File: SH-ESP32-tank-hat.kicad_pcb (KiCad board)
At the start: 4 copper layers, 83 x 55.5 mm, 37 parts, among them J302 GPIO, J303 I2C, J304 Conn_01x02, J305 Power

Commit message: Initial PCB layout
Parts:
- removed the G*** at (78.8, 85.4)
- added C401: 100nF, Capacitor_SMD:C_0402_1005Metric, F.Cu at (107.7, 70.0)
- added C402: 100nF, Capacitor_SMD:C_0402_1005Metric, F.Cu at (107.7, 80.2)
- added C403: 100nF, Capacitor_SMD:C_0402_1005Metric, F.Cu at (122.8, 79.0)
- added C404: 68nF, Capacitor_SMD:C_0603_1608Metric, F.Cu at (127.2, 75.6)
- added C405: 100nF, Capacitor_SMD:C_0402_1005Metric, F.Cu at (107.7, 90.5)
- added C406: 100nF, Capacitor_SMD:C_0402_1005Metric, F.Cu at (107.7, 100.5)
- added C407: 1uF, Capacitor_SMD:C_0402_1005Metric, F.Cu at (118.3, 86.6)
- added C408: 1uF, Capacitor_SMD:C_0402_1005Metric, F.Cu at (115.8, 88.1)
- added C409: 1uF, Capacitor_SMD:C_0402_1005Metric, F.Cu at (115.7, 92.1)
- added C410: 1uF, Capacitor_SMD:C_0402_1005Metric, F.Cu at (117.3, 95.4)
- added C411: 100nF, Capacitor_SMD:C_0402_1005Metric, F.Cu at (118.8, 95.1)
- added C501: 47nF, Capacitor_SMD:C_0603_1608Metric, F.Cu at (133.4, 106.8)
- added C502: 4.7nF, Capacitor_SMD:C_0603_1608Metric, F.Cu at (127.4, 107.0)
- added D501: BZT52C16S, Diode_SMD:D_SOD-323, F.Cu at (131.6, 107.0)
- added J301: GPIO_bottom, Connector_PinSocket_2.54mm:PinSocket_2x20_P2.54mm_Vertical, F.Cu at (167.6, 61.3)
- added J306: Opto, Connector_PinSocket_2.54mm:PinSocket_1x04_P2.54mm_Vertical, B.Cu at (128.3, 113.2)
- added J307: 1-Wire_top, Connector_PinSocket_2.54mm:PinSocket_1x03_P2.54mm_Vertical, F.Cu at (150.3, 102.5)
- added J308: 1-Wire_bottom, Connector_PinSocket_2.54mm:PinSocket_1x03_P2.54mm_Vertical, B.Cu at (150.3, 113.2)
- added J401: Conn_01x02, Connector_Phoenix_MC:PhoenixContact_MCV_1,5_2-G-3.81_1x02_P3.81mm_Vertical, F.Cu at (93.8, 83.0)
- added J402: Conn_01x02, Connector_Phoenix_MC:PhoenixContact_MCV_1,5_2-G-3.81_1x02_P3.81mm_Vertical, F.Cu at (93.8, 72.6)
- added J403: Conn_01x02, Connector_Phoenix_MC:PhoenixContact_MCV_1,5_2-G-3.81_1x02_P3.81mm_Vertical, F.Cu at (93.8, 93.2)
- added J404: Conn_01x02, Connector_Phoenix_MC:PhoenixContact_MCV_1,5_2-G-3.81_1x02_P3.81mm_Vertical, F.Cu at (93.8, 103.4)
- added J501: Conn_01x02, Connector_Phoenix_MC:PhoenixContact_MCV_1,5_2-G-3.81_1x02_P3.81mm_Vertical, F.Cu at (134.4, 100.4)
- added JP501: SolderJumper_2_Open, Jumper:SolderJumper-2_P1.3mm_Open_Pad1.0x1.5mm, F.Cu at (136.2, 108.4)
- added Q401: S9015, Package_TO_SOT_SMD:SOT-23, F.Cu at (103.7, 69.0)
- added Q402: S9015, Package_TO_SOT_SMD:SOT-23, F.Cu at (103.7, 79.2)
- added Q403: S9015, Package_TO_SOT_SMD:SOT-23, F.Cu at (103.7, 89.5)
- added Q404: S9015, Package_TO_SOT_SMD:SOT-23, F.Cu at (103.7, 99.5)
- added R401: 1k, Resistor_SMD:R_0402_1005Metric, F.Cu at (106.7, 70.0)
- added R402: 1k, Resistor_SMD:R_0402_1005Metric, F.Cu at (106.7, 80.2)
- added R403: 30, Resistor_SMD:R_0603_1608Metric, F.Cu at (107.7, 68.0)
- added R404: 30, Resistor_SMD:R_0603_1608Metric, F.Cu at (107.7, 78.2)
- added R405: 1k, Resistor_SMD:R_0402_1005Metric, F.Cu at (129.0, 76.5)
- added R406: 10k, Resistor_SMD:R_0402_1005Metric, F.Cu at (129.0, 75.4)
- added R407: 1k, Resistor_SMD:R_0402_1005Metric, F.Cu at (106.7, 90.5)
- added R408: 1k, Resistor_SMD:R_0402_1005Metric, F.Cu at (106.7, 100.5)
- added R409: 30, Resistor_SMD:R_0603_1608Metric, F.Cu at (107.7, 88.5)
- added R410: 30, Resistor_SMD:R_0603_1608Metric, F.Cu at (107.7, 98.5)
- added R411: 1.5k, Resistor_SMD:R_0402_1005Metric, F.Cu at (117.3, 86.6)
- added R412: 1.5k, Resistor_SMD:R_0402_1005Metric, F.Cu at (115.8, 89.1)
- added R413: 1.5k, Resistor_SMD:R_0402_1005Metric, F.Cu at (115.7, 93.1)
- added R414: 1.5k, Resistor_SMD:R_0402_1005Metric, F.Cu at (117.3, 94.4)
- added R501: 3.3k, Resistor_SMD:R_0805_2012Metric, F.Cu at (129.4, 107.0)
- added U401: LMV324, Package_SO:SOIC-14_3.9x8.7mm_P1.27mm, F.Cu at (117.5, 79.0)
- added U402: ADS1115IDGS, Package_SO:TSSOP-10_3x3mm_P0.5mm, F.Cu at (118.7, 90.7)
- J302: value GPIO -> I2C_top; footprint Connector_PinHeader_2.54mm:PinHeader_2x20_P2.54mm_Vertical -> Connector_PinHeader_2.54mm:PinHeader_1x04_P2.54mm_Vertical
- J303: value I2C -> I2C_bottom; moved to B.Cu
- J304: value Conn_01x02 -> Vin_Prot; footprint Connector_PinHeader_2.54mm:PinHeader_1x02_P2.54mm_Vertical -> Connector_PinSocket_2.54mm:PinSocket_1x02_P2.54mm_Vertical; moved to B.Cu
- J305: footprint Connector_PinHeader_2.54mm:PinHeader_2x03_P2.54mm_Vertical -> Connector_PinSocket_2.54mm:PinSocket_2x03_P2.54mm_Vertical; moved to B.Cu
- moved J302 42.0 mm to (150.3, 97.1)
- turned J303 to 90 degrees
- turned J304 to 270 degrees
- turned J305 to 90 degrees
- renumbered C1001 to C201, C1002 to C202, C1003 to C203, C1004 to C204, C1005 to C205, C1006 to C206, C1007 to C207, C1008 to C208, C1009 to C209, C1010 to C210, C1011 to C211, C1012 to C212, C1013 to C213, C1014 to C214, C1015 to C215, C1016 to C216, C1017 to C217, C1018 to C218, C1019 to C219, C1020 to C220, C1021 to C221, C1022 to C222, C1023 to C223, C1024 to C224, C1025 to C225, C1026 to C226, C1027 to C227, C1028 to C228, H1001 to H201, H1002 to H202
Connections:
- J302 pad 1: (no net) -> GND
- J302 pad 2: (no net) -> +3V3
- J302 pad 3: (no net) -> /SCL
- J302 pad 4: (no net) -> /SDA
- J303 pad 3: (no net) -> /SCL
- J303 pad 4: (no net) -> /SDA
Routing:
- net /Tank sender/VoutA: track 0.00 -> 43.5 mm, vias 0 -> 2
- net /Tank sender/Vin: track 0.00 -> 41.7 mm, vias 0 -> 6
- net /SCL: track 0.00 -> 39.0 mm
- net /SDA: track 0.00 -> 36.3 mm
- net Net-(Q401-Pad1): track 0.00 -> 34.9 mm, vias 0 -> 2
- net /Tank sender/VoutB: track 0.00 -> 33.5 mm, vias 0 -> 4
- net Net-(C401-Pad1): track 0.00 -> 33.2 mm, vias 0 -> 2
- net Net-(Q403-Pad1): track 0.00 -> 31.4 mm, vias 0 -> 2
- net Net-(Q404-Pad1): track 0.00 -> 30.8 mm, vias 0 -> 2
- net /Tank sender/VoutD: track 0.00 -> 30.4 mm, vias 0 -> 2
- net Net-(C406-Pad1): track 0.00 -> 29.6 mm, vias 0 -> 2
- net Net-(C402-Pad1): track 0.00 -> 27.7 mm, vias 0 -> 4
- net /Tank sender/VoutC: track 0.00 -> 26.6 mm, vias 0 -> 2
- net Net-(C405-Pad1): track 0.00 -> 24.0 mm, vias 0 -> 2
- net Net-(Q402-Pad1): track 0.00 -> 22.4 mm, vias 0 -> 2
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- added copper zone on B.Cu, net +3V3
- added copper zone on F.Cu, net GND
- added copper zone on B.Cu, net ISO_GND
- added copper zone on F.Cu, net ISO_GND
- removed copper zone on In2.Cu, net +3V3
- removed copper zone on In1.Cu, net GND
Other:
- board size 83 x 55.5 mm -> 83 x 58 mm
- copper layers 4 -> 2
- board text added: "1Wire"
- board text added: "DQ"
- board text added: "Tach"
- board text added: "Tank A"
- board text added: "Tank B"
- board text added: "Tank C"
- board text added: "Tank D"
- board text removed: "Revision 0.3.0"
- board text removed: "Sailor Hat with ESP32"
- board text removed: "VIn Prot"
- board text removed: "Vin Prot"
- board text removed: "https://github.com/hatlabs/SH-ESP32-hardware/"

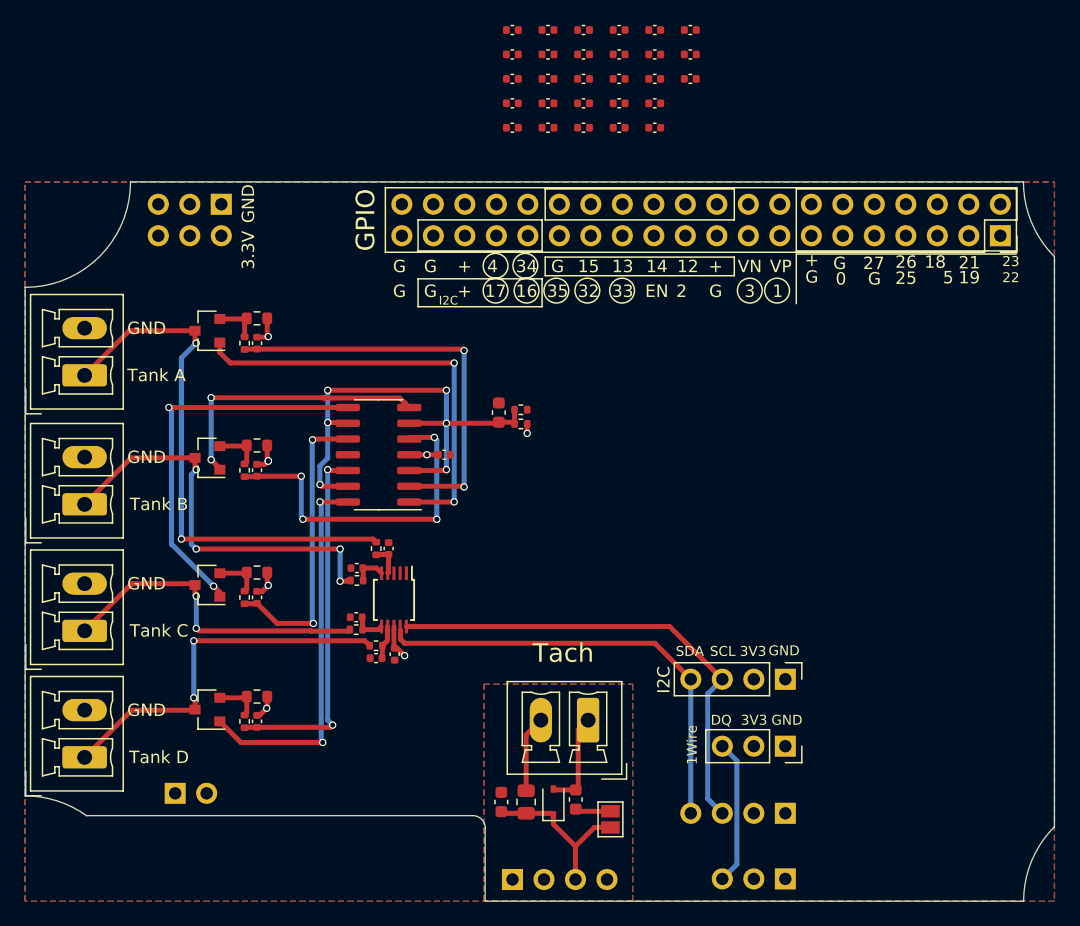
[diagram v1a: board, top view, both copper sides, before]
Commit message: Reduce the PCB size; switch to TLA2024
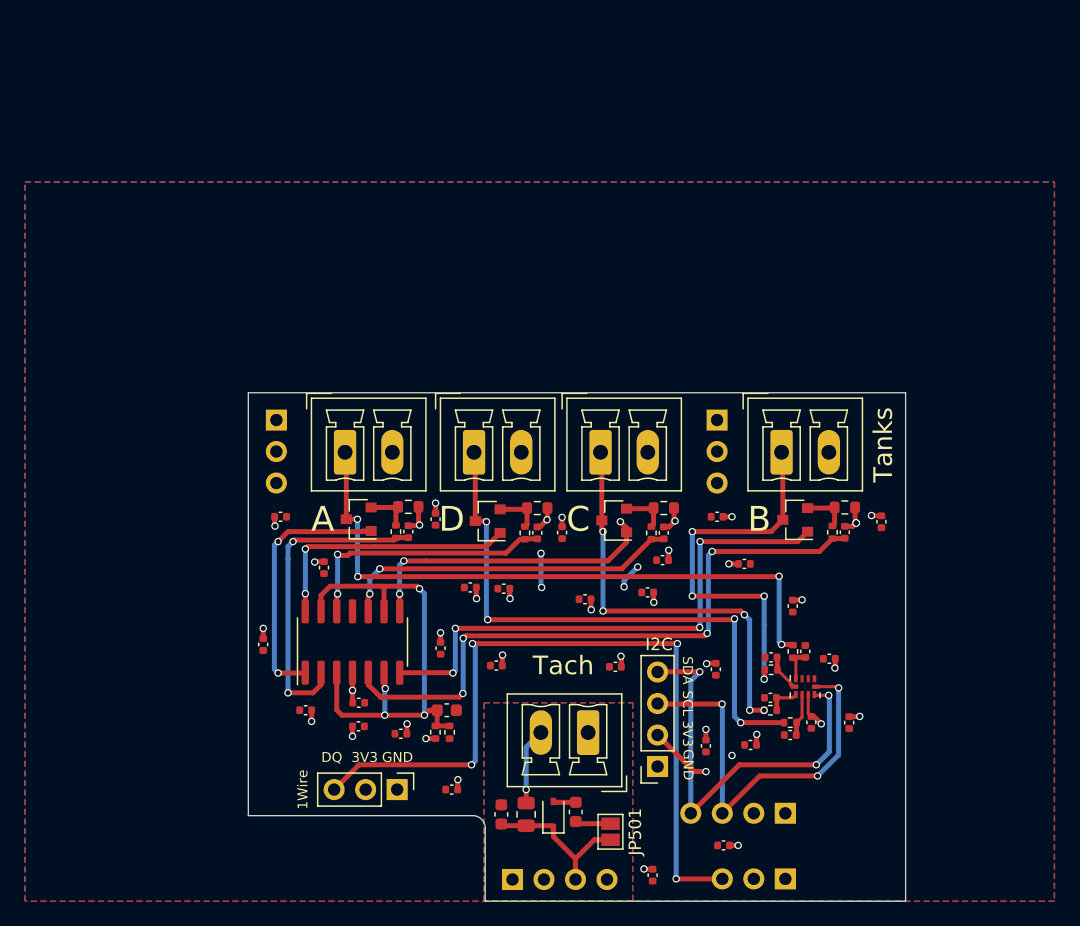
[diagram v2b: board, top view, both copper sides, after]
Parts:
- removed the J302 at (150.3, 97.1)
- removed the J304 at (101.1, 106.3)
- removed the J305 at (104.8, 58.8)
- added J201: Conn_01x03, Connector_PinSocket_2.54mm:PinSocket_1x03_P2.54mm_Vertical, B.Cu at (109.3, 76.2)
- added J202: Conn_01x03, Connector_PinSocket_2.54mm:PinSocket_1x03_P2.54mm_Vertical, B.Cu at (144.8, 76.2)
- J301: value GPIO_bottom -> I2C_top; footprint Connector_PinSocket_2.54mm:PinSocket_2x20_P2.54mm_Vertical -> Connector_PinSocket_2.54mm:PinSocket_1x04_P2.54mm_Vertical
- J304: renamed from J307; footprint Connector_PinSocket_2.54mm:PinSocket_1x03_P2.54mm_Vertical -> Connector_PinHeader_2.54mm:PinHeader_1x03_P2.54mm_Vertical
- U402: value ADS1115IDGS -> TLA2024; footprint Package_SO:TSSOP-10_3x3mm_P0.5mm -> SH-ESP32-tank-hat:Texas_R-PUQFN-N10
- moved C207 67.3 mm to (145.3, 110.5)
- moved C209 66.7 mm to (139.6, 112.9), turned to 90 degrees
- moved C228 60.4 mm to (115.9, 100.9), turned to 180 degrees
- moved C224 57.3 mm to (155.4, 100.6), turned to 90 degrees
- moved J401 56.4 mm to (150.0, 78.8), turned to 0 degrees
- moved C218 55.6 mm to (108.2, 94.3), turned to 90 degrees
- moved C225 54.4 mm to (123.4, 106.0)
- moved C221 52.9 mm to (119.3, 101.5)
- moved C205 52.0 mm to (136.6, 96.1)
- moved J301 50.9 mm to (140.0, 104.1), turned to 180 degrees
- moved C204 50.9 mm to (147.5, 102.4)
- moved C220 50.9 mm to (111.6, 99.6)
- moved C223 50.7 mm to (153.8, 95.5)
- moved C217 50.0 mm to (143.9, 102.5), turned to 90 degrees
- moved C206 49.3 mm to (127.0, 96.0)
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- renumbered J303 to J302, J306 to J303, J308 to J305
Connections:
- J301 pad 1: (no net) -> GND
- J301 pad 2: (no net) -> +3V3
- J301 pad 3: (no net) -> /SCL
- J301 pad 4: (no net) -> /SDA
- U402 pad 3: GND -> (no net)
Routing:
- net /IOHeader/DQ: track 11.7 -> 61.2 mm, vias 0 -> 4
- net +3V3: track 14.8 -> 45.2 mm, vias 8 -> 39
- net Net-(C402-Pad1): track 27.7 -> 51.3 mm
- net Net-(Q402-Pad1): track 22.4 -> 43.8 mm, vias 2 -> 4
- net /Tank sender/VoutD: track 30.4 -> 46.4 mm, vias 2 -> 4
- net Net-(Q401-Pad1): track 34.9 -> 21.2 mm
- net Net-(Q404-Pad1): track 30.8 -> 21.3 mm
- net Net-(C406-Pad1): track 29.6 -> 20.9 mm
- net /Tank sender/VoutA: track 43.5 -> 51.5 mm, vias 2 -> 4
- net Net-(C401-Pad1): track 33.2 -> 25.7 mm
- net /Tank sender/VoutC: track 26.6 -> 33.8 mm, vias 2 -> 5
- net /SCL: track 39.0 -> 32.6 mm, vias 0 -> 3
- net ISO_GND: track 7.71 -> 1.83 mm
- net Net-(Q403-Pad1): track 31.4 -> 25.6 mm, vias 2 -> 3
- net Net-(C405-Pad1): track 24.0 -> 27.7 mm
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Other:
- board size 83 x 58 mm -> 53 x 41 mm
- board text added: "A"
- board text added: "B"
- board text added: "C"
- board text added: "D"
- board text added: "Tanks"
- board text removed: "+"
- board text removed: "0"
- board text removed: "1"
- board text removed: "12"
- board text removed: "13"
- board text removed: "14"
- board text removed: "15"
- board text removed: "16"
- board text removed: "17"
- board text removed: "18"
- board text removed: "19"
- board text removed: "2"
- board text removed: "21"
- board text removed: "22"
- board text removed: "23"
- board text removed: "25"
- board text removed: "26"
- board text removed: "27"
- board text removed: "3"
- board text removed: "3.3V"
- board text removed: "32"
- board text removed: "33"
- board text removed: "34"
- board text removed: "35"
- board text removed: "4"
- board text removed: "5"
- board text removed: "EN"
- board text removed: "G"
- board text removed: "GND & 3.3V"
- board text removed: "GPIO"
- board text removed: "GPIO headers"
- board text removed: "Tank A"
- board text removed: "Tank B"
- board text removed: "Tank C"
- board text removed: "Tank D"
- board text removed: "VN"
- board text removed: "VP"

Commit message: New design with only two channels and using ESP32 internal ADCs
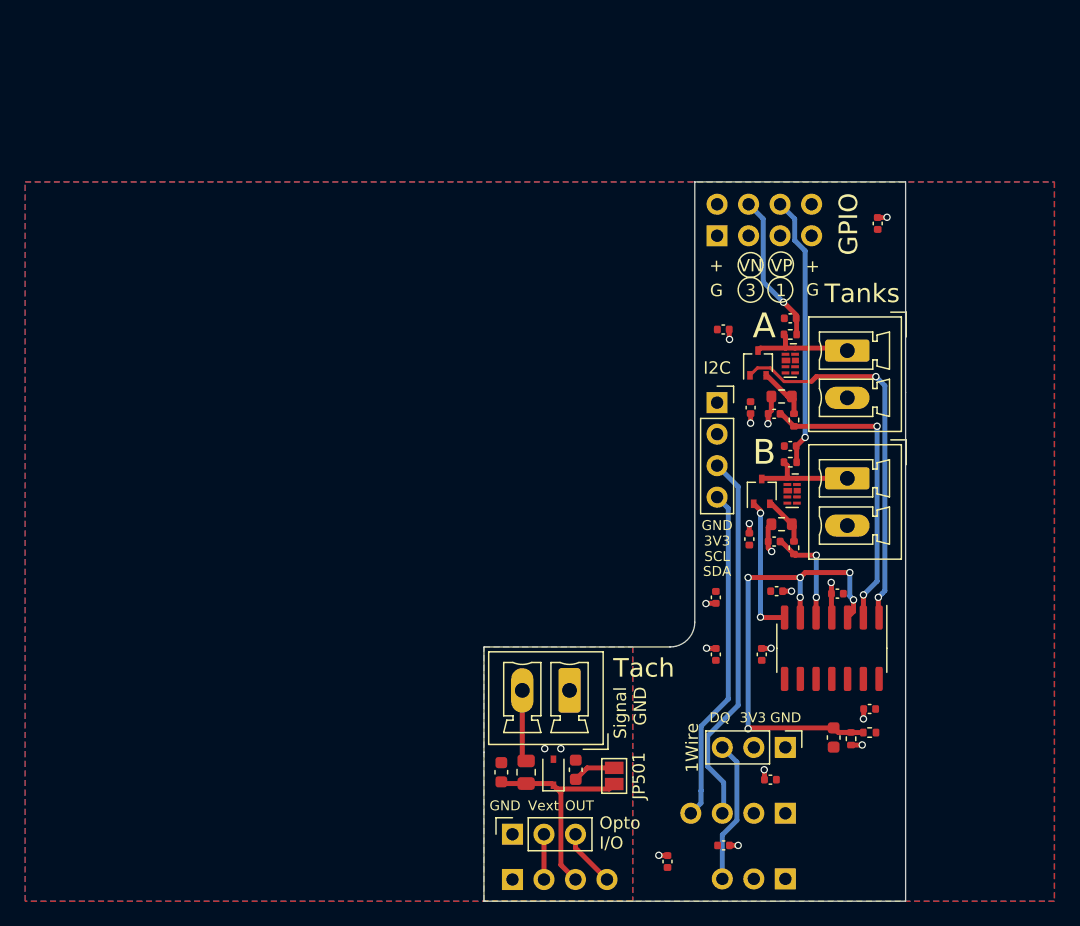
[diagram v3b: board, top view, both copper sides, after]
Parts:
- removed C213, C214, C215, C216, C217, C218, C219, C220, C221, C222, C223, C224, C225, C226, C227, C228, C411: 100nF, Capacitor_SMD:C_0402_1005Metric
- removed C407, C408, C409, C410: 1uF, Capacitor_SMD:C_0402_1005Metric
- removed J201, J202: Conn_01x03, Connector_PinSocket_2.54mm:PinSocket_1x03_P2.54mm_Vertical
- removed the J304 at (119.0, 106.0)
- removed J403, J404: Conn_01x02, Connector_Phoenix_MC:PhoenixContact_MCV_1,5_2-G-3.81_1x02_P3.81mm_Vertical
- removed Q403, Q404: S9015, Package_TO_SOT_SMD:SOT-23
- removed R409, R410: 30, Resistor_SMD:R_0603_1608Metric
- removed R411, R412, R413, R414: 1.5k, Resistor_SMD:R_0402_1005Metric
- added J303: GPIO subset, Connector_PinSocket_2.54mm:PinSocket_2x04_P2.54mm_Vertical, B.Cu at (144.8, 61.3)
- added J305: 1-Wire_top, Connector_PinHeader_2.54mm:PinHeader_1x03_P2.54mm_Vertical, F.Cu at (150.3, 102.6)
- added J307: Opto_top, Connector_PinSocket_2.54mm:PinSocket_1x03_P2.54mm_Vertical, F.Cu at (128.3, 109.6)
- added U403: RCLAMP0524P-N, Package_DFN_QFN:Diodes_UDFN-10_1.0x2.5mm_P0.5mm, F.Cu at (150.8, 81.9)
- C405, C406: value 100nF -> 1uF
- J304: renamed from J303; value Opto -> Opto_bottom
- Q401, Q402: footprint Package_TO_SOT_SMD:SOT-23 -> Package_TO_SOT_SMD:SOT-323_SC-70
- R407, R408: value 1k -> 1.5k
- U402: value TLA2024 -> RCLAMP0524P-N; footprint SH-ESP32-tank-hat:Texas_R-PUQFN-N10 -> Package_DFN_QFN:Diodes_UDFN-10_1.0x2.5mm_P0.5mm
- moved REF** 75.6 mm to (154.1, 95.7)
- moved G*** 62.2 mm to (141.7, 97.4)
- moved C206 47.1 mm to (157.8, 60.4), turned to 90 degrees
- moved J401 41.3 mm to (155.3, 70.6), turned to 270 degrees
- moved C403 39.6 mm to (154.5, 90.2)
- moved U401 38.7 mm to (154.1, 94.6), turned to 270 degrees
- moved C211 36.8 mm to (144.7, 95.1), turned to 90 degrees
- moved C201 36.0 mm to (148.4, 95.1)
- moved Q401 34.6 mm to (148.1, 71.6), turned to 90 degrees
- moved R406 33.9 mm to (157.1, 101.4), turned to 0 degrees
- moved R405 33.5 mm to (155.6, 101.9)
- moved R401 33.3 mm to (151.0, 76.2)
- moved R403 31.4 mm to (150.0, 74.3), turned to 0 degrees
- moved C404 31.3 mm to (154.2, 101.8), turned to 270 degrees
- moved C401 31.0 mm to (149.4, 75.7), turned to 180 degrees
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- renumbered J305 to J306, J402 to J401, J401 to J402
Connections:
- C405 pad 1: Net-(C405-Pad1) -> /IOHeader/ADC_A
- C405 pad 2: +3V3 -> GND
- C406 pad 1: Net-(C406-Pad1) -> /IOHeader/ADC_B
- C406 pad 2: +3V3 -> GND
- J301 pad 3: /SCL -> /IOHeader/SCL
- J301 pad 4: /SDA -> /IOHeader/SDA
- J302 pad 3: /SCL -> /IOHeader/SCL
- J302 pad 4: /SDA -> /IOHeader/SDA
- J304 pad 2: (no net) -> /IOHeader/V_ISO
- J304 pad 4: (no net) -> /IOHeader/ISO_OUT
- R407 pad 1: Net-(Q403-Pad2) -> /IOHeader/ADC_A
- R407 pad 2: Net-(C405-Pad1) -> /Tank sender/VoutA
- R408 pad 1: Net-(Q404-Pad2) -> /IOHeader/ADC_B
- R408 pad 2: Net-(C406-Pad1) -> /Tank sender/VoutB
- U401 pad 10: Net-(C405-Pad1) -> GND
- U401 pad 12: Net-(C406-Pad1) -> GND
- U401 pad 13: /Tank sender/Vin -> GND
- U401 pad 14: Net-(Q404-Pad1) -> (no net)
- U401 pad 8: Net-(Q403-Pad1) -> (no net)
- U401 pad 9: /Tank sender/Vin -> GND
- U402 pad 1: GND -> /Tank sender/VoutA
- U402 pad 10: /SCL -> /Tank sender/VoutA
- U402 pad 3: (no net) -> GND
- U402 pad 4: /Tank sender/VadcA -> (no net)
- U402 pad 5: /Tank sender/VadcB -> (no net)
- U402 pad 6: /Tank sender/VadcC -> (no net)
- U402 pad 7: /Tank sender/VadcD -> (no net)
- U402 pad 8: +3V3 -> GND
- U402 pad 9: /SDA -> (no net)
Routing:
- net /IOHeader/DQ: track 61.2 -> 11.6 mm, vias 4 -> 0
- net /Tank sender/VoutD: track 46.4 -> 0.00 mm, vias 4 -> 0
- net /Tank sender/VoutA: track 51.5 -> 8.52 mm, vias 4 -> 0
- net Net-(C402-Pad1): track 51.3 -> 8.41 mm, vias 4 -> 2
- net /SDA: track 34.1 -> 0.00 mm, vias 3 -> 0
- net /Tank sender/VoutC: track 33.8 -> 0.00 mm, vias 5 -> 0
- net /SCL: track 32.6 -> 0.00 mm, vias 3 -> 0
- net Net-(Q402-Pad1): track 43.8 -> 11.3 mm, vias 4 -> 2
- net /IOHeader/SCL: track 0.00 -> 30.3 mm
- net Net-(C405-Pad1): track 27.7 -> 0.00 mm, vias 2 -> 0
- net +3V3: track 45.2 -> 17.7 mm, vias 39 -> 16
- net /IOHeader/SDA: track 0.00 -> 27.1 mm
- net Net-(Q403-Pad1): track 25.6 -> 0.00 mm, vias 3 -> 0
- net /Tank sender/VoutB: track 31.8 -> 8.33 mm, vias 4 -> 0
- net /IOHeader/ADC_B: track 0.00 -> 22.0 mm, vias 0 -> 1
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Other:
- board size 53 x 41 mm -> 34 x 58 mm
- board text added: "+"
- board text added: "1"
- board text added: "3"
- board text added: "G"
- board text added: "GPIO"
- board text added: "OUT"
- board text added: "Opto I/O"
- board text added: "Signal GND"
- board text added: "VN"
- board text added: "VP"
- board text added: "Vext"
- board text removed: "ANTENNA-KEEP OUT"
- board text removed: "C"
- board text removed: "D"
